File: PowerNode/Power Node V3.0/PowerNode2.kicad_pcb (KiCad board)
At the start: 2 copper layers, 78.4 x 64.8 mm, 66 parts, among them IC1 ACS712xLCTR-30A, IC2 74HC595N, IC3 CD4511B, IC4 CD4511B

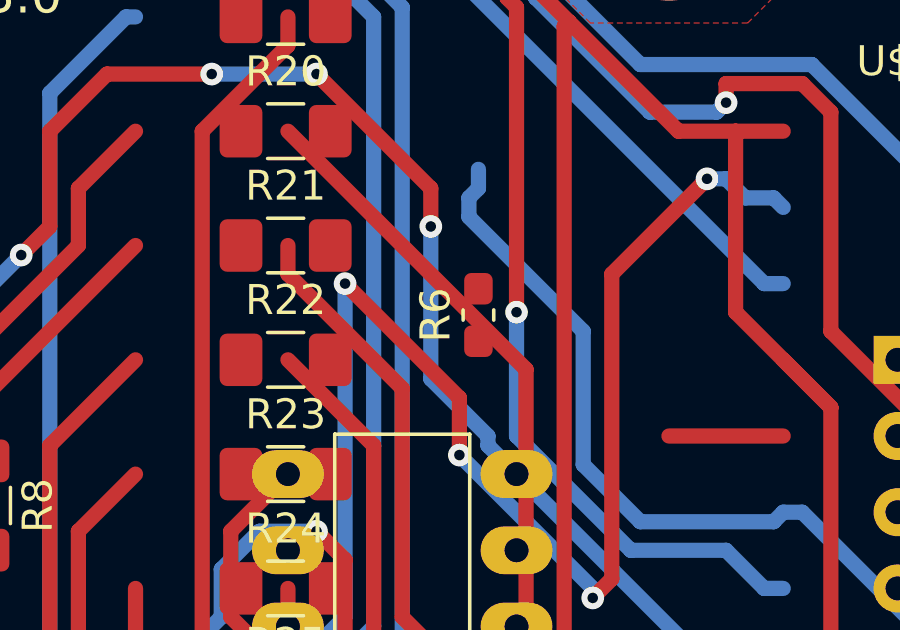
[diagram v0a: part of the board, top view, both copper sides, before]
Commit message: PN3: removed extra low-pass filter from IMEAS
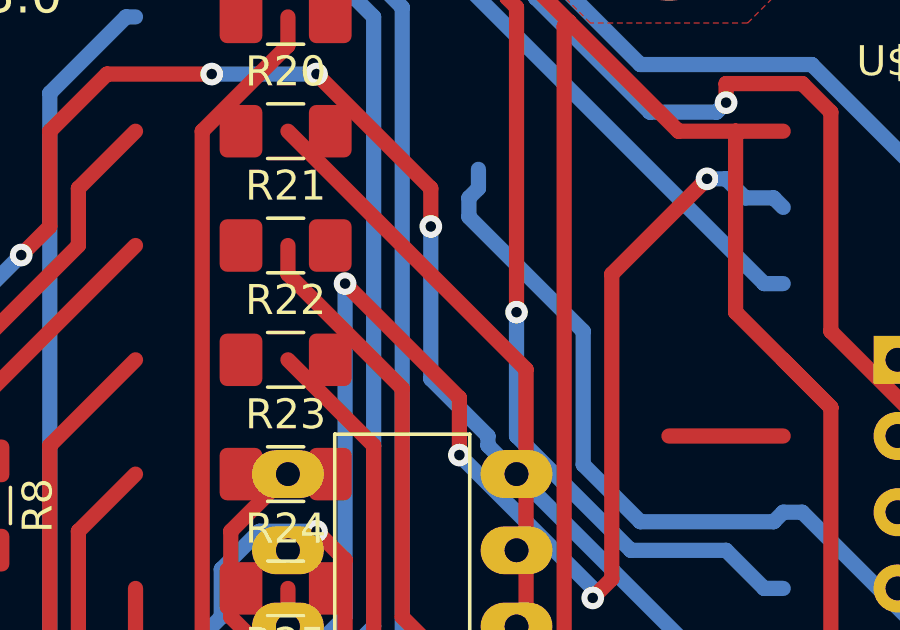
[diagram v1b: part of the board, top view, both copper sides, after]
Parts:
- removed R6: 10k, Resistor_SMD:R_0603_1608Metric_Pad1.05x0.95mm_HandSolder
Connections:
- IC1 pad 7: Net-(IC1-Pad7) -> /IMEAS
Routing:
- net /IMEAS: track 0.00 -> 59.8 mm
- net Net-(IC1-Pad7): track 78.4 -> 18.6 mm
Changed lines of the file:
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@@
     (drawings 10)
     (tracks 658)
-    (modules 66)
+    (modules 65)
     (nets 109)
   )
@@
     )
   )
-  (module "Resistor_SMD:R_0603_1608Metric_Pad1.05x0.95mm_HandSolder" (layer "Top")
-    (at 157.5561 101.6 90)
-    (descr "Resistor SMD 0603 (1608 Metric), square (rectangular) end terminal, IPC_7351 nominal with elongated pad for handsoldering. (Body size source: http://www.tortai-tech.com/upload/download/2011102023233369053.pdf), generated with kicad-footprint-generator")
-    (tags "resistor handsolder")
-    (attr smd)
-    (fp_text reference "R6" (at 0 -1.43 90) (layer "F.SilkS")
-      (effects (font (size 1 1) (thickness 0.15)))
-    )
-    (fp_text value "10k" (at 0 1.43 90) (layer "F.Fab")
-      (effects (font (size 1 1) (thickness 0.15)))
-    )
-    (fp_line (start -0.8 0.4) (end -0.8 -0.4) (layer "F.Fab") (width 0.1))
-    (fp_line (start -0.8 -0.4) (end 0.8 -0.4) (layer "F.Fab") (width 0.1))
-    (fp_line (start 0.8 -0.4) (end 0.8 0.4) (layer "F.Fab") (width 0.1))
-    (fp_line (start 0.8 0.4) (end -0.8 0.4) (layer "F.Fab") (width 0.1))
-    (fp_line (start -0.171267 -0.51) (end 0.171267 -0.51) (layer "F.SilkS") (width 0.12))
-    (fp_line (start -0.171267 0.51) (end 0.171267 0.51) (layer "F.SilkS") (width 0.12))
-    (fp_line (start -1.65 0.73) (end -1.65 -0.73) (layer "F.CrtYd") (width 0.05))
-    (fp_line (start -1.65 -0.73) (end 1.65 -0.73) (layer "F.CrtYd") (width 0.05))
-    (fp_line (start 1.65 -0.73) (end 1.65 0.73) (layer "F.CrtYd") (width 0.05))
-    (fp_line (start 1.65 0.73) (end -1.65 0.73) (layer "F.CrtYd") (width 0.05))
-    (fp_text user "%R" (at 0 0 90) (layer "F.Fab")
-      (effects (font (size 0.4 0.4) (thickness 0.06)))
-    )
-    (pad "2" smd roundrect (at 0.875 0 90) (size 1.05 0.95) (layers "Top" "F.Paste" "F.Mask") (roundrect_rratio 0.25)
-      (net 46 "/IMEAS"))
-    (pad "1" smd roundrect (at -0.875 0 90) (size 1.05 0.95) (layers "Top" "F.Paste" "F.Mask") (roundrect_rratio 0.25)
-      (net 18 "Net-(IC1-Pad7)"))
-    (model "${KISYS3DMOD}/Resistor_SMD.3dshapes/R_0603_1608Metric.wrl"
-      (at (xyz 0 0 0))
-      (scale (xyz 1 1 1))
-      (rotate (xyz 0 0 0))
-    )
-  )
   (module "Resistor_SMD:R_1206_3216Metric_Pad1.42x1.75mm_HandSolder" (layer "Top")
     (at 171.01 64.26)
@@
       (net 44 "Vdd"))
     (pad "7" smd roundrect (at 2.475 -0.635 270) (size 1.95 0.6) (layers "Top" "F.Paste" "F.Mask") (roundrect_rratio 0.25)
-      (net 18 "Net-(IC1-Pad7)"))
+      (net 46 "/IMEAS"))
     (pad "6" smd roundrect (at 2.475 0.635 270) (size 1.95 0.6) (layers "Top" "F.Paste" "F.Mask") (roundrect_rratio 0.25)
       (net 9 "Net-(C1-Pad1)"))
@@
   (segment (start 180.7336 112.9361) (end 182.3211 114.5236) (width 0.508) (layer "Bottom") (net 44))
   (segment (start 182.3211 114.5236) (end 182.9561 114.5236) (width 0.508) (layer "Bottom") (net 44))
-  (segment (start 173.4311 83.0911) (end 173.4311 82.8336) (width 0.508) (layer "Top") (net 18) (status 30))
-  (segment (start 173.7486 83.4086) (end 173.4311 83.0911) (width 0.508) (layer "Top") (net 18) (status 20))
-  (segment (start 173.7486 84.3611) (end 173.7486 83.4086) (width 0.508) (layer "Top") (net 18))
-  (segment (start 175.3361 85.9486) (end 173.7486 84.3611) (width 0.508) (layer "Top") (net 18))
-  (segment (start 186.1311 85.9486) (end 175.3361 85.9486) (width 0.508) (layer "Top") (net 18))
-  (segment (start 186.1311 99.6011) (end 186.1311 85.9486) (width 0.508) (layer "Top") (net 18))
-  (segment (start 184.5436 101.1886) (end 186.1311 99.6011) (width 0.508) (layer "Top") (net 18))
-  (segment (start 178.1936 101.1886) (end 184.5436 101.1886) (width 0.508) (layer "Top") (net 18))
-  (segment (start 178.1936 96.1086) (end 178.1936 101.1886) (width 0.508) (layer "Top") (net 18))
-  (segment (start 175.9711 93.8861) (end 178.1936 96.1086) (width 0.508) (layer "Top") (net 18))
-  (segment (start 173.7486 93.8861) (end 175.9711 93.8861) (width 0.508) (layer "Top") (net 18))
-  (segment (start 173.7486 104.0461) (end 173.7486 93.8861) (width 0.508) (layer "Top") (net 18))
-  (segment (start 175.3361 105.6336) (end 173.7486 104.0461) (width 0.508) (layer "Top") (net 18))
+  (segment (start 173.4311 83.0911) (end 173.4311 82.8336) (width 0.508) (layer "Top") (net 46) (status 30))
+  (segment (start 173.7486 83.4086) (end 173.4311 83.0911) (width 0.508) (layer "Top") (net 46) (status 20))
+  (segment (start 173.7486 84.3611) (end 173.7486 83.4086) (width 0.508) (layer "Top") (net 46))
+  (segment (start 175.3361 85.9486) (end 173.7486 84.3611) (width 0.508) (layer "Top") (net 46))
+  (segment (start 186.1311 85.9486) (end 175.3361 85.9486) (width 0.508) (layer "Top") (net 46))
+  (segment (start 186.1311 99.6011) (end 186.1311 85.9486) (width 0.508) (layer "Top") (net 46))
+  (segment (start 184.5436 101.1886) (end 186.1311 99.6011) (width 0.508) (layer "Top") (net 46))
+  (segment (start 178.1936 101.1886) (end 184.5436 101.1886) (width 0.508) (layer "Top") (net 46))
+  (segment (start 178.1936 96.1086) (end 178.1936 101.1886) (width 0.508) (layer "Top") (net 46))
+  (segment (start 175.9711 93.8861) (end 178.1936 96.1086) (width 0.508) (layer "Top") (net 46))
+  (segment (start 173.7486 93.8861) (end 175.9711 93.8861) (width 0.508) (layer "Top") (net 46))
+  (segment (start 173.7486 104.0461) (end 173.7486 93.8861) (width 0.508) (layer "Top") (net 46))
+  (segment (start 175.3361 105.6336) (end 173.7486 104.0461) (width 0.508) (layer "Top") (net 46))
   (segment (start 143.5861 131.9861) (end 139.4586 136.1136) (width 0.508) (layer "Bottom") (net 45) (status 10))
   (segment (start 139.4586 136.1136) (end 128.9811 136.1136) (width 0.508) (layer "Bottom") (net 45))

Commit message: PN3: changed LEDs to SMD and VOLT1 to bi-color, other small changes
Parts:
- removed VDIV1: LED5MM, LED_THT:LED_D5.0mm
- added R6: 220, Resistor_SMD:R_1206_3216Metric_Pad1.42x1.75mm_HandSolder, F.Cu at (151.9, 44.2)
- added VPASS1: LED, LED_SMD:LED_0603_1608Metric_Pad1.05x0.95mm_HandSolder, F.Cu at (119.4, 64.5)
- IC2: value 74HC595N -> 74HC594N
- PWR1: value LED5MM -> LED; footprint LED_THT:LED_D5.0mm -> LED_SMD:LED_0603_1608Metric_Pad1.05x0.95mm_HandSolder
- VOLT1: value LED5MM -> HSMF-C173; footprint LED_THT:LED_D5.0mm -> HSMFC173:HSMFC173
- moved VOLT1 63.8 mm to (131.6, 45.7), turned to 0 degrees
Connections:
- S1 pad 1: Vss -> Vdd
- S1 pad 3: Vdd -> Vss
- VOLT1 pad 1: Net-(R8-Pad2) -> /SWITCH
- VOLT1 pad 2: /SWITCH -> Net-(R8-Pad2)
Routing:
- net /VCC: track 210.3 -> 157.9 mm
- net Vdd: track 54.6 -> 107.0 mm

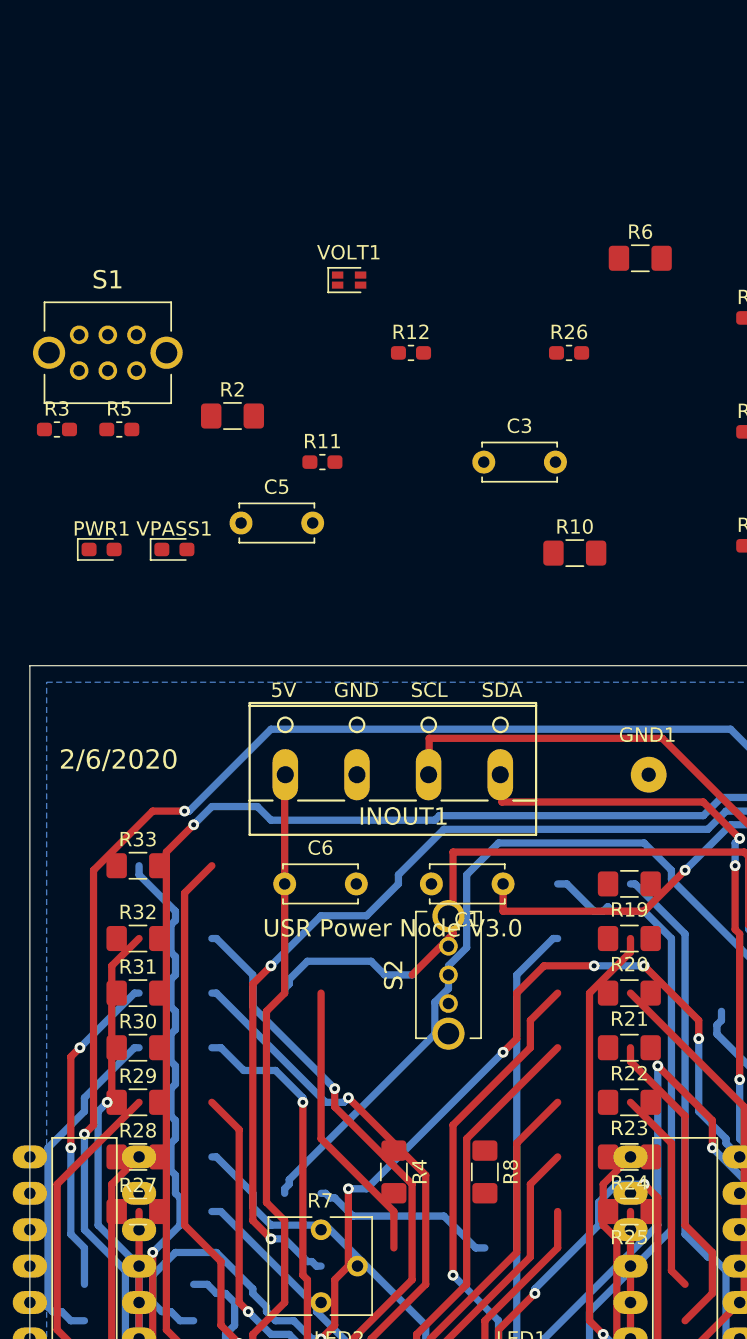
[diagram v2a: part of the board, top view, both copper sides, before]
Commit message: PN3: changed to resistor networks from drivers and footprint/model cleanup
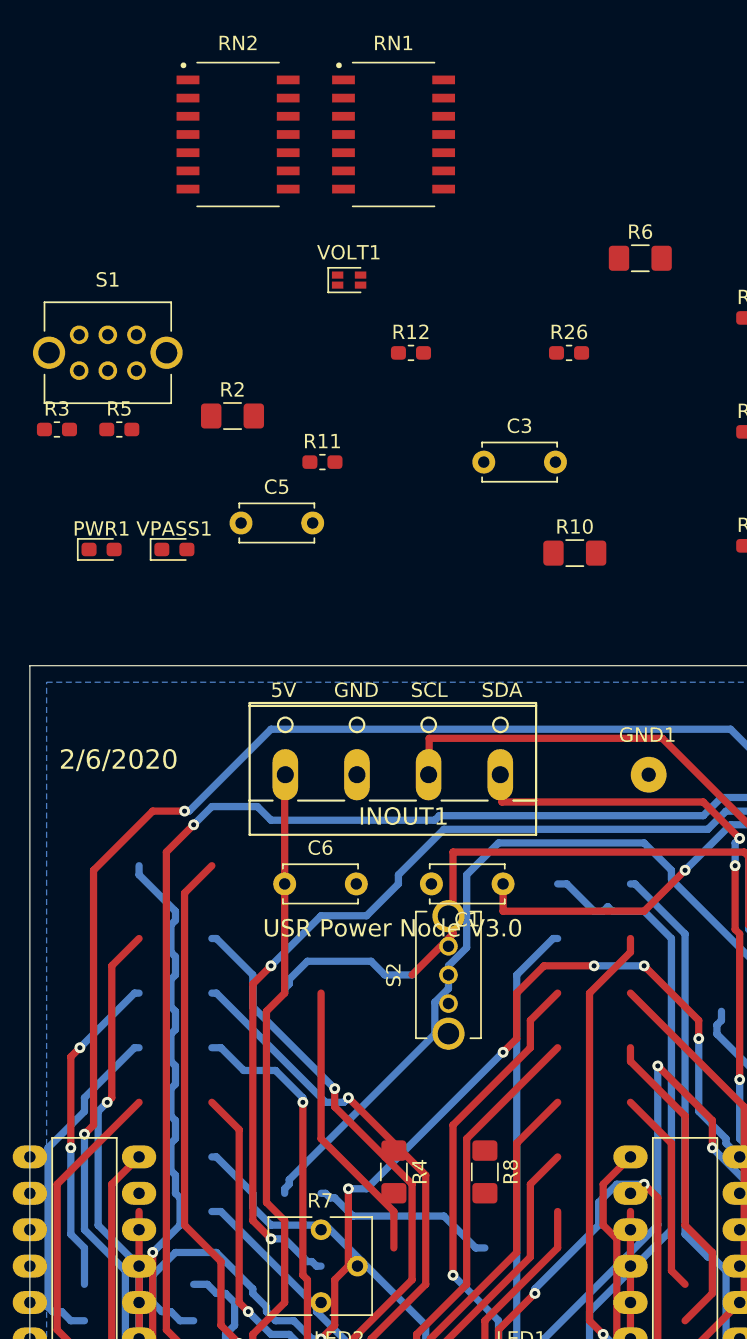
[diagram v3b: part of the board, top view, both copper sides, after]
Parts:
- removed R19, R20, R21, R22, R23, R24, R25, R27, R28, R29, R30, R31, R32, R33: 220, Resistor_SMD:R_1206_3216Metric_Pad1.42x1.75mm_HandSolder
- added RN1: 220, PowerNode2:SOIC127P762X240-14N, F.Cu at (134.7, 35.6)
- added RN2: 220, PowerNode2:SOIC127P762X240-14N, F.Cu at (123.8, 35.6)
- S1: footprint OSx02011MS2Qx1:OS202011MS2Qx1 -> PowerNode2:OS202011MS2Qx1
- S2: footprint OSx02011MS2Qx1:OS102011MS2Qx1 -> PowerNode2:OS102011MS2Qx1
- VOLT1: footprint HSMFC173:HSMFC173 -> PowerNode2:HSMFC173
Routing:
- net Net-(IC7-Pad12): track 18.1 -> 0.00 mm
- net Vss: track 30.0 -> 48.1 mm

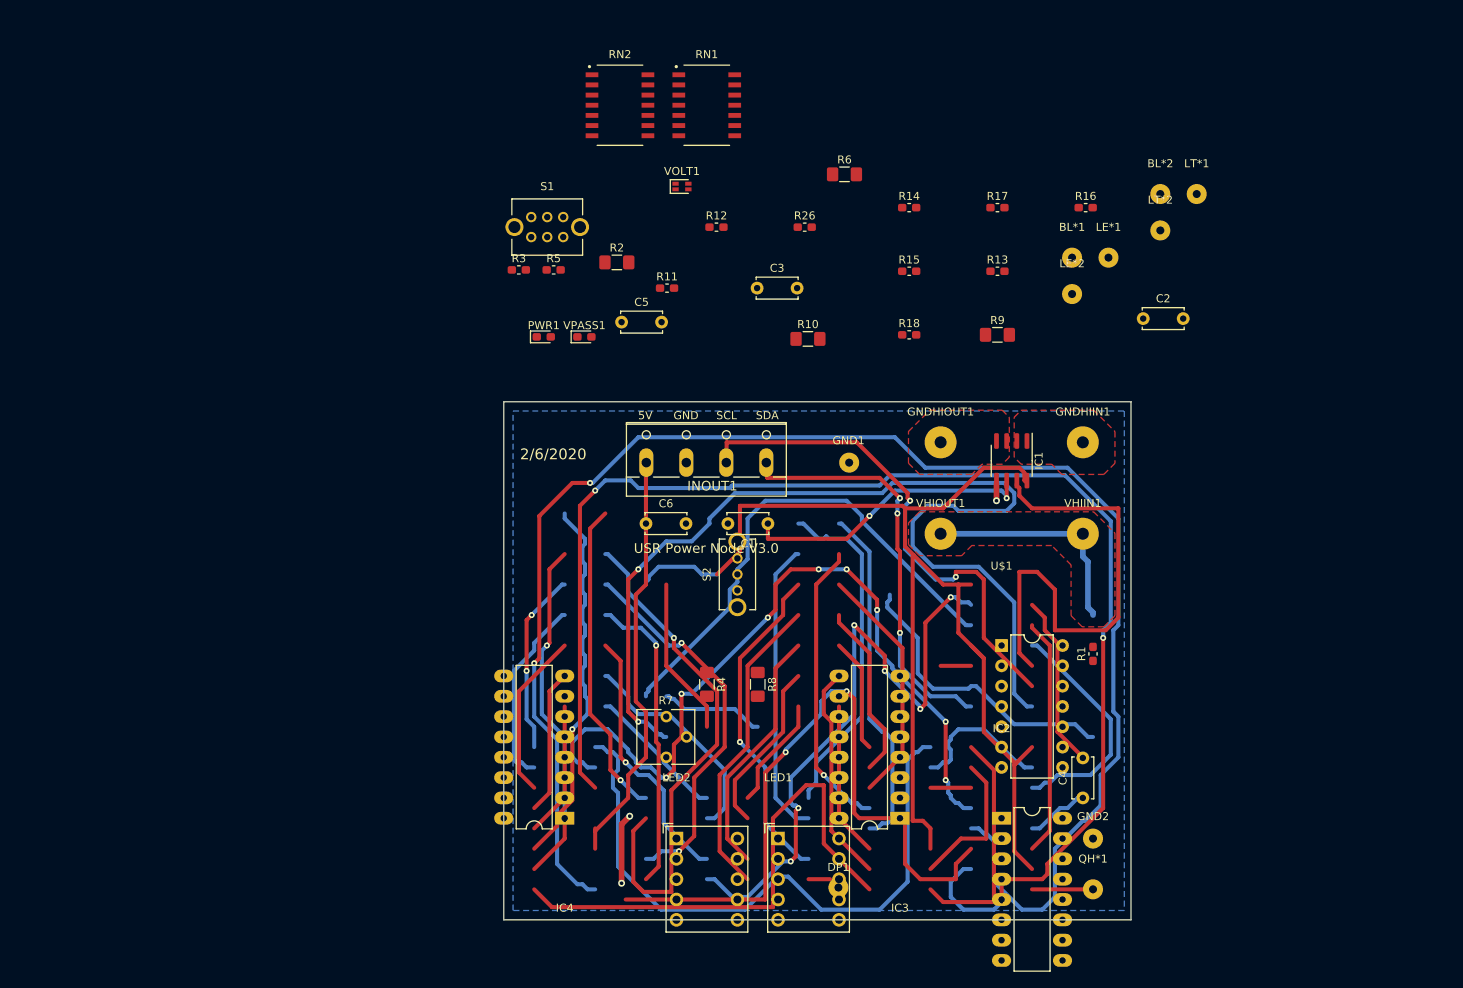
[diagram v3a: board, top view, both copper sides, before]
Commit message: PN3: Started routing and made appropriate adjustments
One noteworthy adjustment was switching the VMEAS and VPOT pins
on the ATTiny. The slave code was also updated.
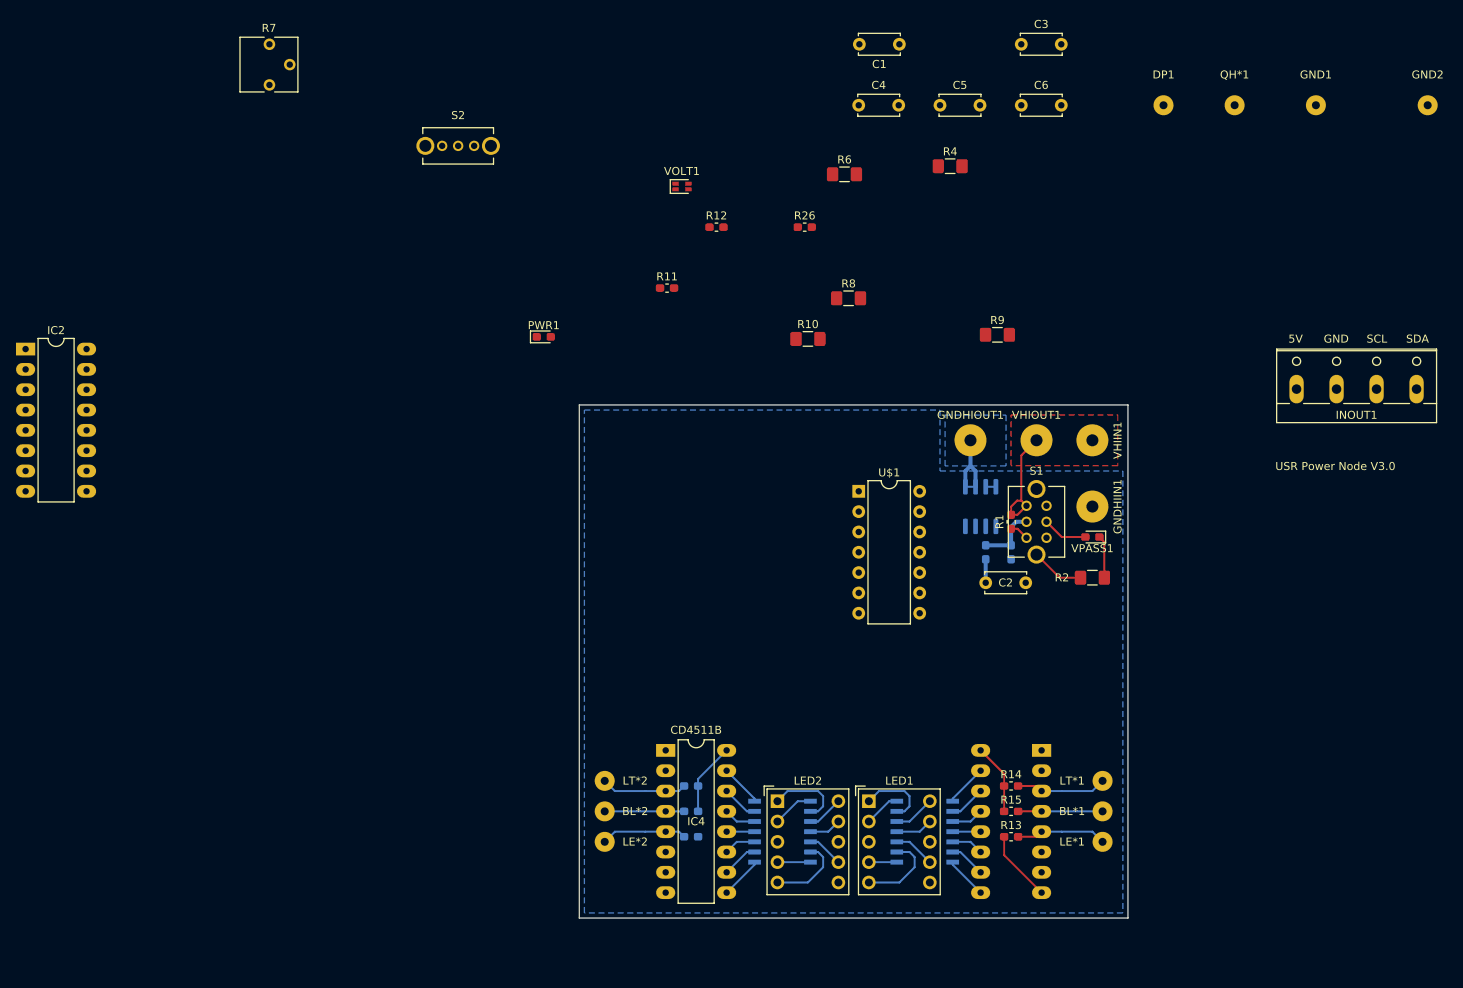
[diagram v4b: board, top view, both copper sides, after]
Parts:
- IC1, IC3, R16, R17, R18, R3, R5, RN1, RN2: moved to B.Cu
- moved IC2 135.4 mm to (49.5, 66.0)
- moved DP1 105.9 mm to (191.8, 35.6)
- moved BL*2 103.8 mm to (121.9, 123.8)
- moved GND2 100.8 mm to (224.8, 35.6)
- moved QH*1 99.6 mm to (200.7, 35.6)
- moved LT*2 97.8 mm to (121.9, 120.0)
- moved R7 97.6 mm to (80.0, 33.0)
- moved RN1 94.8 mm to (161.9, 126.4)
- moved RN2 93.1 mm to (144.1, 126.4)
- moved R16 92.8 mm to (132.7, 127.0), turned to 180 degrees
- moved C4 91.0 mm to (153.7, 35.6), turned to 0 degrees
- moved LE*2 90.0 mm to (121.9, 127.6)
- moved R17 81.8 mm to (132.7, 120.7), turned to 180 degrees
- moved INOUT1 81.7 mm to (215.9, 71.1)
- moved LT*1 74.3 mm to (184.2, 120.0)
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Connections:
- net /VDIV renamed /VPASS
- net Net-(GNDHIOUT1-Pad1) renamed /GNDHIOUT
- RN1 pad 1: Net-(IC3-Pad9) -> /e1
- RN1 pad 10: /a1 -> Net-(IC3-Pad13)
- RN1 pad 11: /b1 -> Net-(IC3-Pad12)
- RN1 pad 12: /c1 -> Net-(IC3-Pad11)
- RN1 pad 13: /d1 -> Net-(IC3-Pad10)
- RN1 pad 14: /e1 -> Net-(IC3-Pad9)
- RN1 pad 2: Net-(IC3-Pad10) -> /d1
- RN1 pad 3: Net-(IC3-Pad11) -> /c1
- RN1 pad 4: Net-(IC3-Pad12) -> /b1
- RN1 pad 5: Net-(IC3-Pad13) -> /a1
- RN1 pad 6: Net-(IC3-Pad14) -> /g1
- RN1 pad 7: Net-(IC3-Pad15) -> /f1
- RN1 pad 8: /f1 -> Net-(IC3-Pad15)
- RN1 pad 9: /g1 -> Net-(IC3-Pad14)
- S1 pad 7: (no net) -> Vss
- S1 pad 8: (no net) -> Vss
- S2 pad 4: (no net) -> Vss
- S2 pad 5: (no net) -> Vss
- U$1 pad 6: /VMEAS_1 -> /VPOT
- U$1 pad 8: /VPOT -> /VMEAS_1
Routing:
- net Net-(IC5-Pad5): track 201.3 -> 0.00 mm
- net Net-(IC5-Pad7): track 175.9 -> 0.00 mm
- net /VCC: track 157.9 -> 0.00 mm
- net /VPOT: track 125.2 -> 0.00 mm, vias 2 -> 0
- net Net-(IC5-Pad4): track 97.8 -> 0.00 mm
- net Vdd: track 107.0 -> 17.9 mm
- net Net-(IC5-Pad6): track 88.5 -> 0.00 mm
- net GND: track 79.6 -> 0.00 mm
- net Net-(LED2-Pad6): track 79.4 -> 0.00 mm
- net Net-(LED1-Pad9): track 65.3 -> 0.00 mm
- net Net-(LED2-Pad2): track 64.5 -> 0.00 mm
- net /SCL: track 63.6 -> 0.00 mm, vias 2 -> 0
- net /SWITCH: track 63.2 -> 0.00 mm
- net /IMEAS: track 59.8 -> 0.00 mm
- net /SDA: track 51.9 -> 0.00 mm, vias 3 -> 0
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- added copper zone on B.Cu, net /GNDHIOUT
- added copper zone on F.Cu, net /VHI
- added copper zone on B.Cu, net Vss
- removed copper zone on F.Cu, net /GNDHIOUT
- removed copper zone on B.Cu, net Net-(C1-Pad2)
- removed copper zone on F.Cu, net Net-(C1-Pad2)
- removed copper zone on F.Cu, net Net-(R2-Pad2)
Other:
- board size 78.4 x 64.8 mm -> 68.6 x 64.1 mm
- board text removed: "2/6/2020"
- board text removed: "5V"
- board text removed: "GND"
- board text removed: "SCL"
- board text removed: "SDA"
